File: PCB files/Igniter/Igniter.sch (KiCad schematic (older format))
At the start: 26 parts, among them J1 PT2, J2 PT1, J3 PT4, J4 PT3, J5 Conn_01x02_Female, J6 IgnitionCoil, J7 SD Header, Q1 N MOSFET, SW1 ARM, SW3 Ignite

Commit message: 10/31/2019
Text edits
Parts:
- J5: value Conn_01x02_Female -> Battery
- R?: value 1k -> 10k
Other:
- moved on the sheet: F1, J5
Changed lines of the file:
@@
 L power:GNDREF #PWR01
 U 1 1 5DA63712
-P 9710 1505
-F 0 "#PWR01" H 9710 1255 50  0001 C CNN
-F 1 "GNDREF" H 9715 1332 50  0001 C CNN
-F 2 "" H 9710 1505 50  0001 C CNN
-F 3 "" H 9710 1505 50  0001 C CNN
-	1    9710 1505
+P 9670 1510
+F 0 "#PWR01" H 9670 1260 50  0001 C CNN
+F 1 "GNDREF" H 9675 1337 50  0001 C CNN
+F 2 "" H 9670 1510 50  0001 C CNN
+F 3 "" H 9670 1510 50  0001 C CNN
+	1    9670 1510
 	1    0    0    -1
 $EndComp
@@
 L Connector:Conn_01x02_Female J5
 U 1 1 5DAB9C23
-P 9910 1385
-F 0 "J5" H 9937 1361 50  0000 L CNN
-F 1 "Conn_01x02_Female" H 9937 1270 50  0001 L CNN
-F 2 "" H 9910 1385 50  0001 C CNN
-F 3 "~" H 9910 1385 50  0001 C CNN
-	1    9910 1385
+P 9870 1390
+F 0 "J5" H 9897 1366 50  0000 L CNN
+F 1 "Battery" H 9897 1275 50  0000 L CNN
+F 2 "" H 9870 1390 50  0001 C CNN
+F 3 "~" H 9870 1390 50  0001 C CNN
+	1    9870 1390
 	1    0    0    -1
 $EndComp
@@
 L Device:Fuse F1
 U 1 1 5DB57AA9
-P 9155 1200
-F 0 "F1" H 9215 1246 50  0000 L CNN
-F 1 "Fuse" H 9215 1155 50  0000 L CNN
-F 2 "Resistor_THT:R_Axial_DIN0204_L3.6mm_D1.6mm_P5.08mm_Horizontal" V 9085 1200 50  0001 C CNN
-F 3 "~" H 9155 1200 50  0001 C CNN
-	1    9155 1200
-	1    0    0    -1
-$EndComp
-Wire Wire Line
-	9710 1505 9710 1485
+P 9115 1205
+F 0 "F1" H 9175 1251 50  0000 L CNN
+F 1 "Fuse" H 9175 1160 50  0000 L CNN
+F 2 "Resistor_THT:R_Axial_DIN0204_L3.6mm_D1.6mm_P5.08mm_Horizontal" V 9045 1205 50  0001 C CNN
+F 3 "~" H 9115 1205 50  0001 C CNN
+	1    9115 1205
+	1    0    0    -1
+$EndComp
+Wire Wire Line
+	9670 1510 9670 1490
 $Comp
 L power:+5V #PWR0101
@@
 AR Path="/5DBA787B" Ref="R?"  Part="1"
 F 0 "R?" V 2698 2260 50  0001 C CNN
-F 1 "1k" V 2900 2260 50  0000 C CNN
+F 1 "10k" V 2900 2260 50  0000 C CNN
 F 2 "Resistor_THT:R_Axial_DIN0204_L3.6mm_D1.6mm_P5.08mm_Horizontal" V 2835 2260 50  0001 C CNN
 F 3 "~" H 2905 2260 50  0001 C CNN
@@
 	2905 2410 2905 2460
 Wire Wire Line
-	9635 1385 9710 1385
-Text Notes 8995 1235 0    50   ~ 0
+	9595 1390 9670 1390
+Text Notes 8955 1240 0    50   ~ 0
 5A
 $Comp
@@
 L power:+24V #PWR?
 U 1 1 5DBB64EE
-P 9155 1050
-F 0 "#PWR?" H 9155 900 50  0001 C CNN
-F 1 "+24V" H 9170 1223 50  0000 C CNN
-F 2 "" H 9155 1050 50  0001 C CNN
-F 3 "" H 9155 1050 50  0001 C CNN
-	1    9155 1050
+P 9115 1055
+F 0 "#PWR?" H 9115 905 50  0001 C CNN
+F 1 "+24V" H 9130 1228 50  0000 C CNN
+F 2 "" H 9115 1055 50  0001 C CNN
+F 3 "" H 9115 1055 50  0001 C CNN
+	1    9115 1055
 	1    0    0    -1
 $EndComp
@@
 L Switch:SW_SPST SW?
 U 1 1 5DAB7506
-P 9435 1385
+P 9395 1390
 AR Path="/5D9BEB88/5DAB7506" Ref="SW?"  Part="1"
 AR Path="/5DAB7506" Ref="SW1"  Part="1"
-F 0 "SW1" H 9435 1160 50  0001 C CNN
-F 1 "ARM" H 9435 1510 50  0000 C CNN
-F 2 "" H 9435 1385 50  0001 C CNN
-F 3 "~" H 9435 1385 50  0001 C CNN
-	1    9435 1385
+F 0 "SW1" H 9395 1165 50  0001 C CNN
+F 1 "ARM" H 9395 1515 50  0000 C CNN
+F 2 "" H 9395 1390 50  0001 C CNN
+F 3 "~" H 9395 1390 50  0001 C CNN
+	1    9395 1390
 	-1   0    0    1
 $EndComp
 Wire Wire Line
-	9155 1385 9235 1385
-Wire Wire Line
-	9155 1385 9155 1350
+	9115 1390 9195 1390
+Wire Wire Line
+	9115 1390 9115 1355
 Wire Notes Line
 	8750 1635 10205 1635

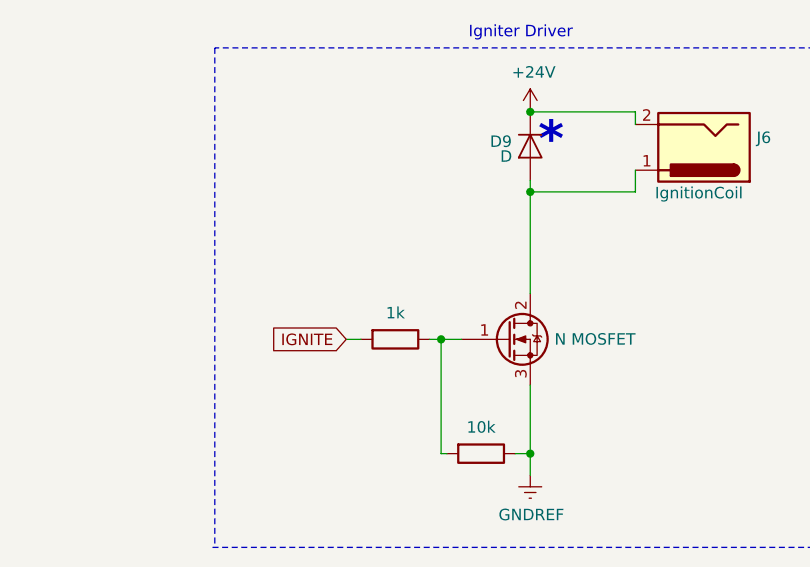
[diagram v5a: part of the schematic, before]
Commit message: 10/31/2019
-Updated and added footprints
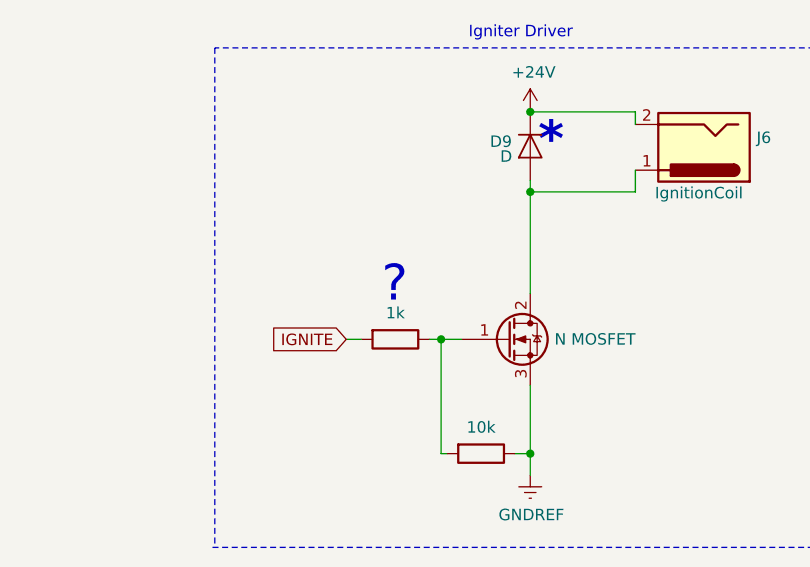
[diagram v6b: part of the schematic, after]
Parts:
- D9: footprint (none) -> Diode_THT:D_DO-15_P12.70mm_Horizontal
- gave numbers to parts that had none: 1
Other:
- note added: "?"
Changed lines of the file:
@@
 P 2905 2260
 AR Path="/5D9BEB88/5DBA787B" Ref="R?"  Part="1"
-AR Path="/5DBA787B" Ref="R?"  Part="1"
-F 0 "R?" V 2698 2260 50  0001 C CNN
+AR Path="/5DBA787B" Ref="R2"  Part="1"
+F 0 "R2" V 2698 2260 50  0001 C CNN
 F 1 "10k" V 2900 2260 50  0000 C CNN
 F 2 "Resistor_THT:R_Axial_DIN0204_L3.6mm_D1.6mm_P5.08mm_Horizontal" V 2835 2260 50  0001 C CNN
@@
 $EndComp
 $Comp
-L power:GNDREF #PWR?
+L power:GNDREF #PWR0107
 U 1 1 5DBA8069
 P 2905 2460
-F 0 "#PWR?" H 2905 2210 50  0001 C CNN
+F 0 "#PWR0107" H 2905 2210 50  0001 C CNN
 F 1 "GNDREF" H 2910 2287 50  0001 C CNN
 F 2 "" H 2905 2460 50  0001 C CNN
@@
 F 0 "D9" V 8865 4875 50  0000 L CNN
 F 1 "D" V 8930 4874 50  0000 L CNN
-F 2 "" H 8885 4795 50  0001 C CNN
+F 2 "Diode_THT:D_DO-15_P12.70mm_Horizontal" H 8885 4795 50  0001 C CNN
 F 3 "~" H 8885 4795 50  0001 C CNN
 	1    8885 4795
@@
 	9345 4645 8885 4645
 $Comp
-L power:+24V #PWR?
+L power:+24V #PWR0109
 U 1 1 5DBB64EE
 P 9115 1055
-F 0 "#PWR?" H 9115 905 50  0001 C CNN
+F 0 "#PWR0109" H 9115 905 50  0001 C CNN
 F 1 "+24V" H 9130 1228 50  0000 C CNN
 F 2 "" H 9115 1055 50  0001 C CNN
@@
 $EndComp
 $Comp
-L power:+24V #PWR?
+L power:+24V #PWR0111
 U 1 1 5DBB6589
 P 9850 2360
-F 0 "#PWR?" H 9850 2210 50  0001 C CNN
+F 0 "#PWR0111" H 9850 2210 50  0001 C CNN
 F 1 "+24V" H 9865 2533 50  0000 C CNN
 F 2 "" H 9850 2360 50  0001 C CNN
@@
 $EndComp
 $Comp
-L power:+24V #PWR?
+L power:+24V #PWR0113
 U 1 1 5DBB7502
 P 8885 4645
-F 0 "#PWR?" H 8885 4495 50  0001 C CNN
+F 0 "#PWR0113" H 8885 4495 50  0001 C CNN
 F 1 "+24V" H 8900 4818 50  0000 C CNN
 F 2 "" H 8885 4645 50  0001 C CNN
@@
 Wire Notes Line
 	8750 1635 10205 1635
+Text Notes 8235 5495 0    157  ~ 0
+?
 $EndSCHEMATC

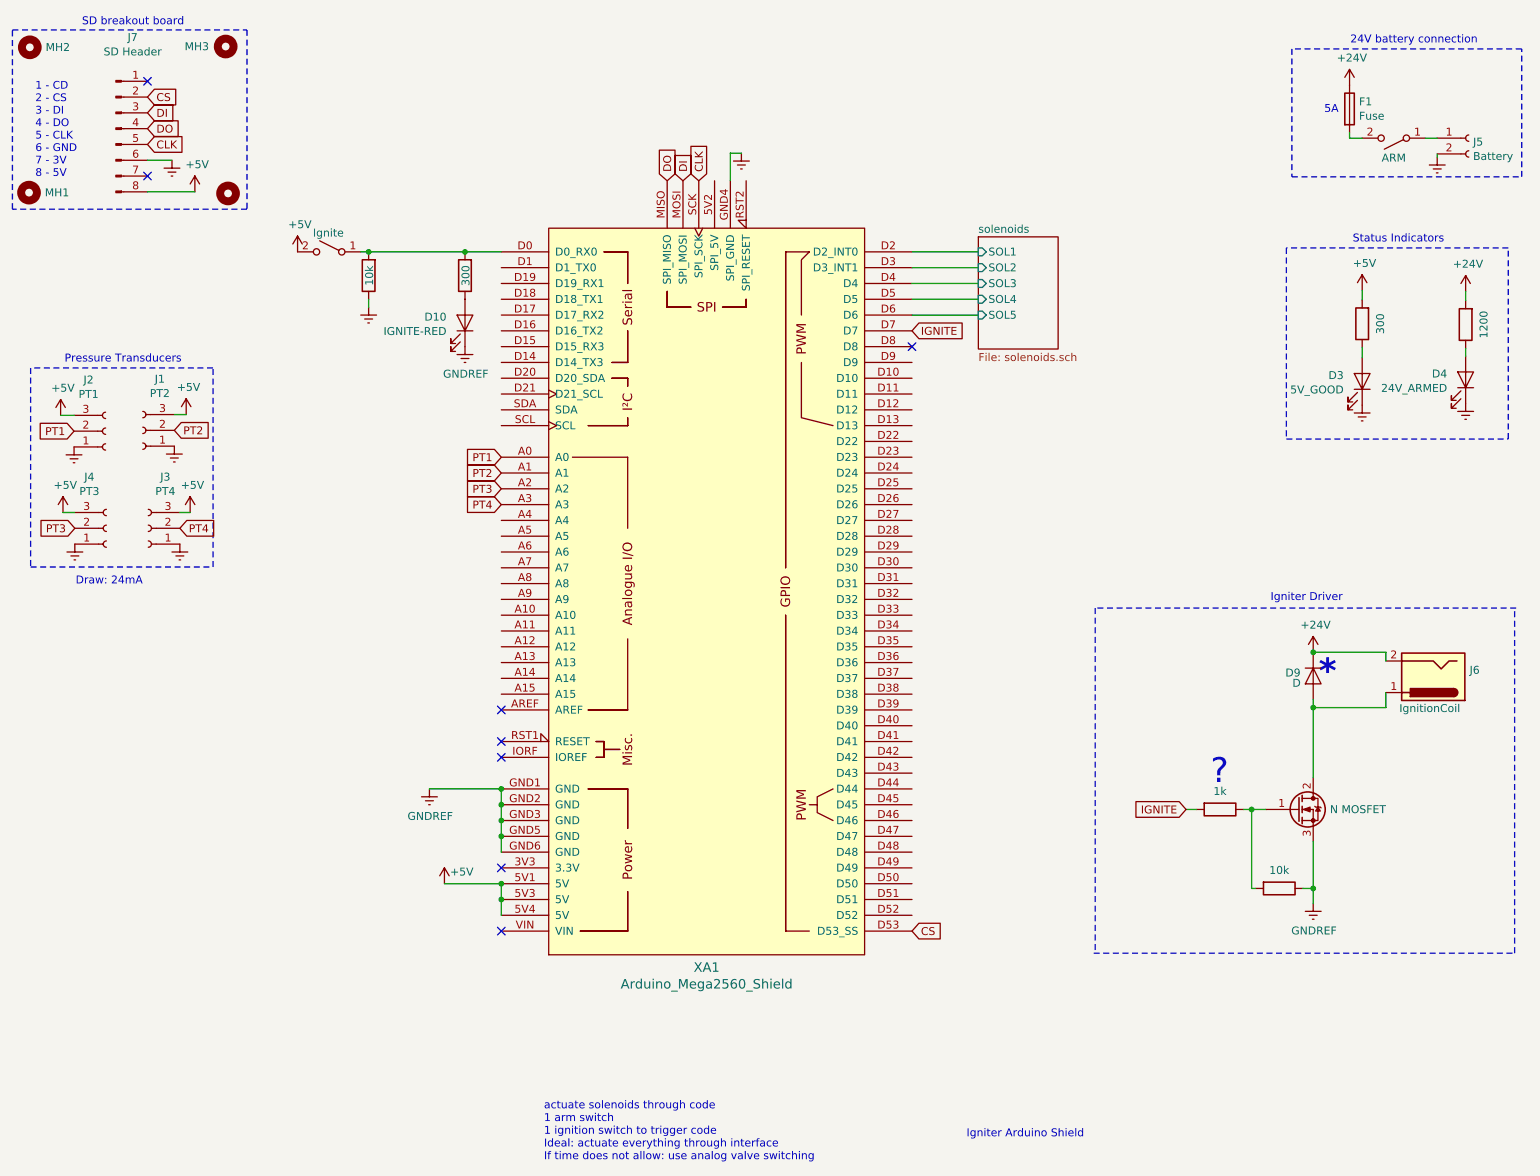
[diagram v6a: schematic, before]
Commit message: 11/1/2019
-Created bananajack footprint
-Began arranging components on board
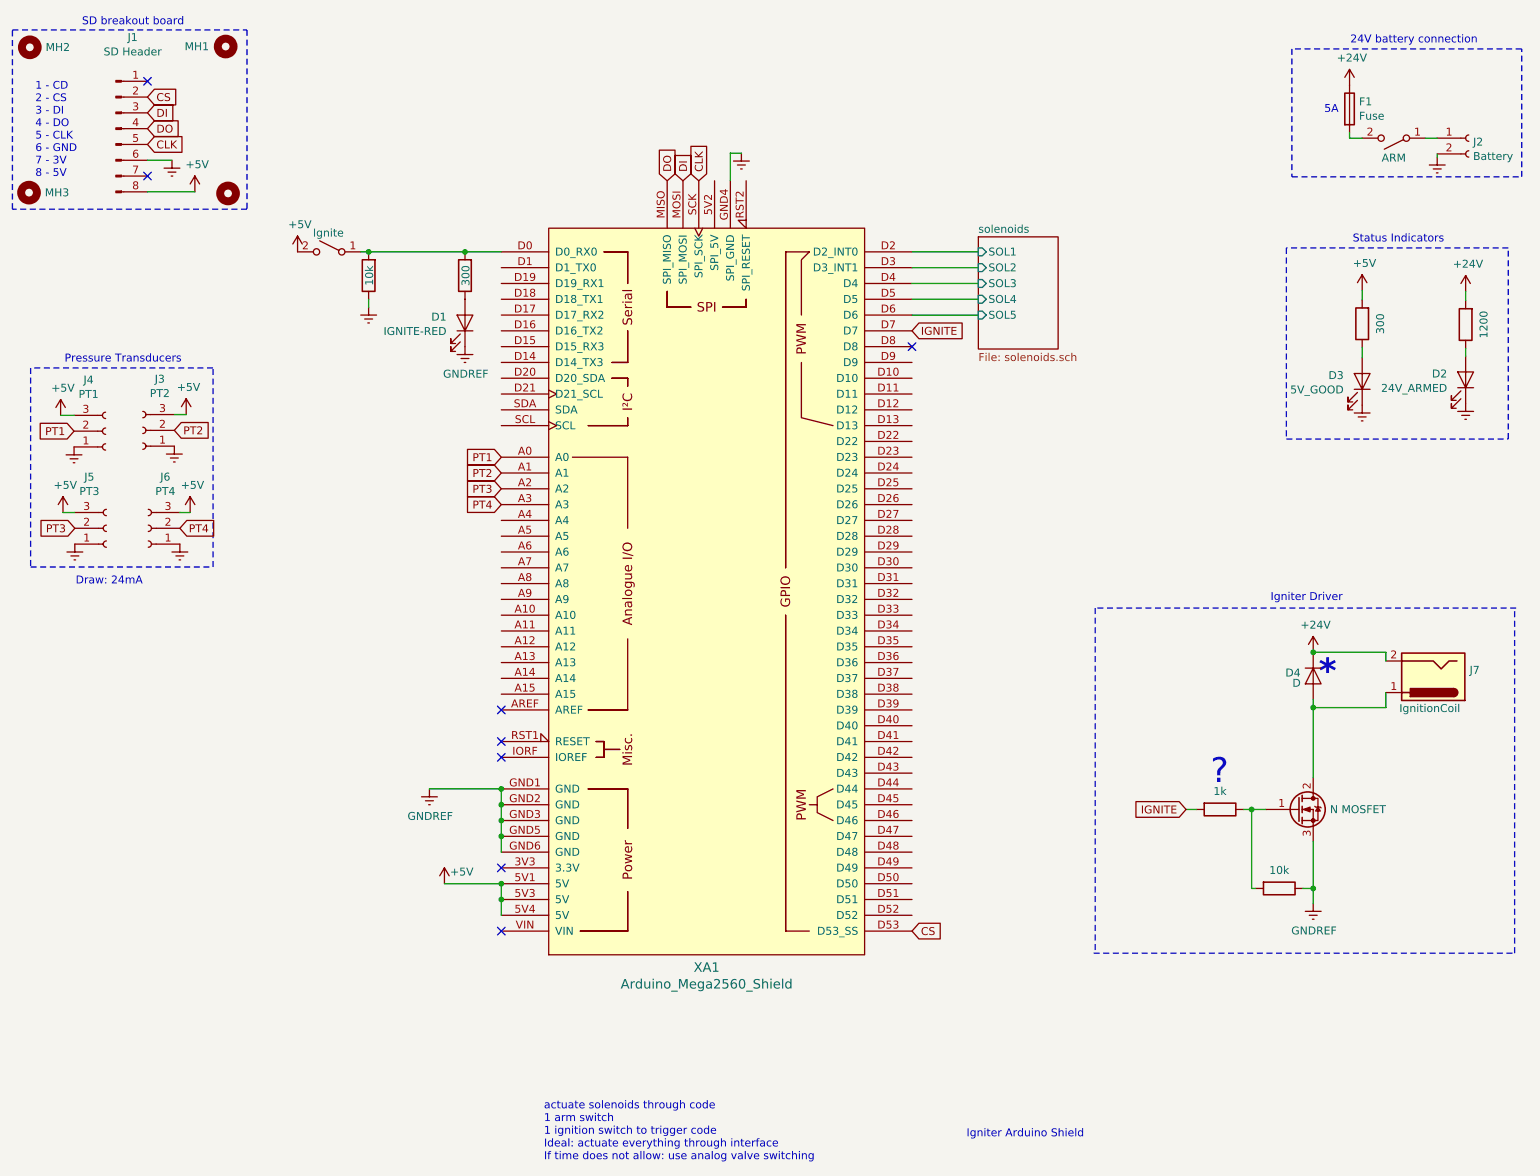
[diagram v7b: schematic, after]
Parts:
- J2: renamed from J5; footprint (none) -> Igniter:BananaJack15.5mm
- J7: renamed from J6; footprint Connector:Banana_Jack_2Pin -> Igniter:BananaJack15.5mm
- renumbered D10 to D1, D4 to D2, D9 to D4, J7 to J1, J1 to J3, J2 to J4, J4 to J5, J3 to J6, MH3 to MH1, MH1 to MH3, R2 to R1, R4 to R2, R5 to R3, R6 to R4, R1 to R5, R3 to R6, SW3 to SW2

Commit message: 11/2/2019
-Started making custom fuse holder footprint
-Selecting more component footprints
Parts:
- F1: footprint Resistor_THT:R_Axial_DIN0204_L3.6mm_D1.6mm_P5.08mm_Horizontal -> IgniterCustom:FuseHolder
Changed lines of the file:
@@
 LIBS:interface
 LIBS:Igniter-cache
-EELAYER 29 0
+EELAYER 26 0
 EELAYER END
 $Descr A 11000 8500
@@
 F 0 "F1" H 9175 1251 50  0000 L CNN
 F 1 "Fuse" H 9175 1160 50  0000 L CNN
-F 2 "Resistor_THT:R_Axial_DIN0204_L3.6mm_D1.6mm_P5.08mm_Horizontal" V 9045 1205 50  0001 C CNN
+F 2 "IgniterCustom:FuseHolder" V 9045 1205 50  0001 C CNN
 F 3 "~" H 9115 1205 50  0001 C CNN
 	1    9115 1205
